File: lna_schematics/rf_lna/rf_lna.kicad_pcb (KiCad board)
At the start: 4 copper layers, 26 parts, among them J1 Conn_01x02_Pin, J2 Conn_Coaxial_Small, J3 Conn_Coaxial_Small, U1 L78L05_SOT89, U2 BFP640, U3 BFP640, U4 BFP640

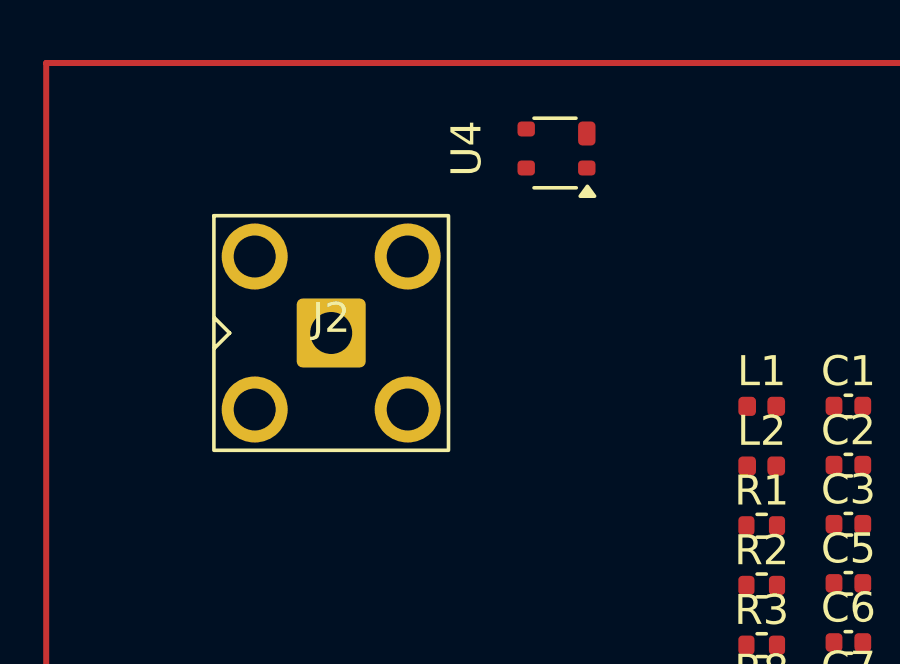
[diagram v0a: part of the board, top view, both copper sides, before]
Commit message: [kicad] Implemement custom design rule for CPW
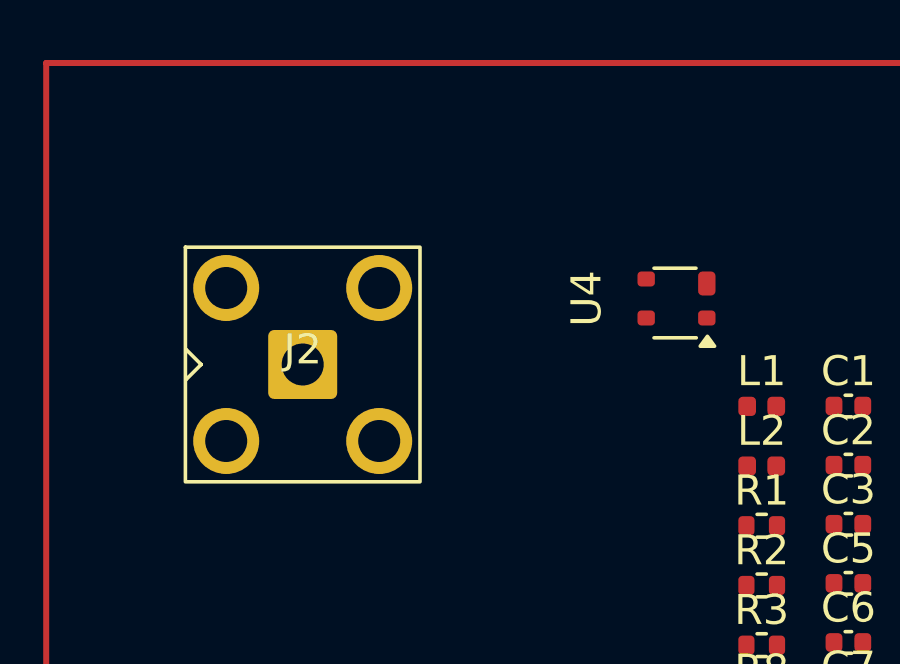
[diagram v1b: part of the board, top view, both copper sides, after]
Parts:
- moved U4 6.40 mm to (71.0, 57.9)
- moved J2 1.42 mm to (58.5, 60.0)
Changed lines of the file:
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@@
 	(footprint "Library:BFP640"
 		(layer "F.Cu")
-		(at 67.01 52.85 90)
+		(at 71.01 57.85 90)
 		(property "Reference" "U4"
 			(at 0 -3 90)
@@
 	(footprint "Library:SMA_Amphenol_901-143_Vertical"
 		(layer "F.Cu")
-		(at 59.5 59)
+		(at 58.55 60.05)
 		(property "Reference" "J2"
 			(at 0 -0.5 0)

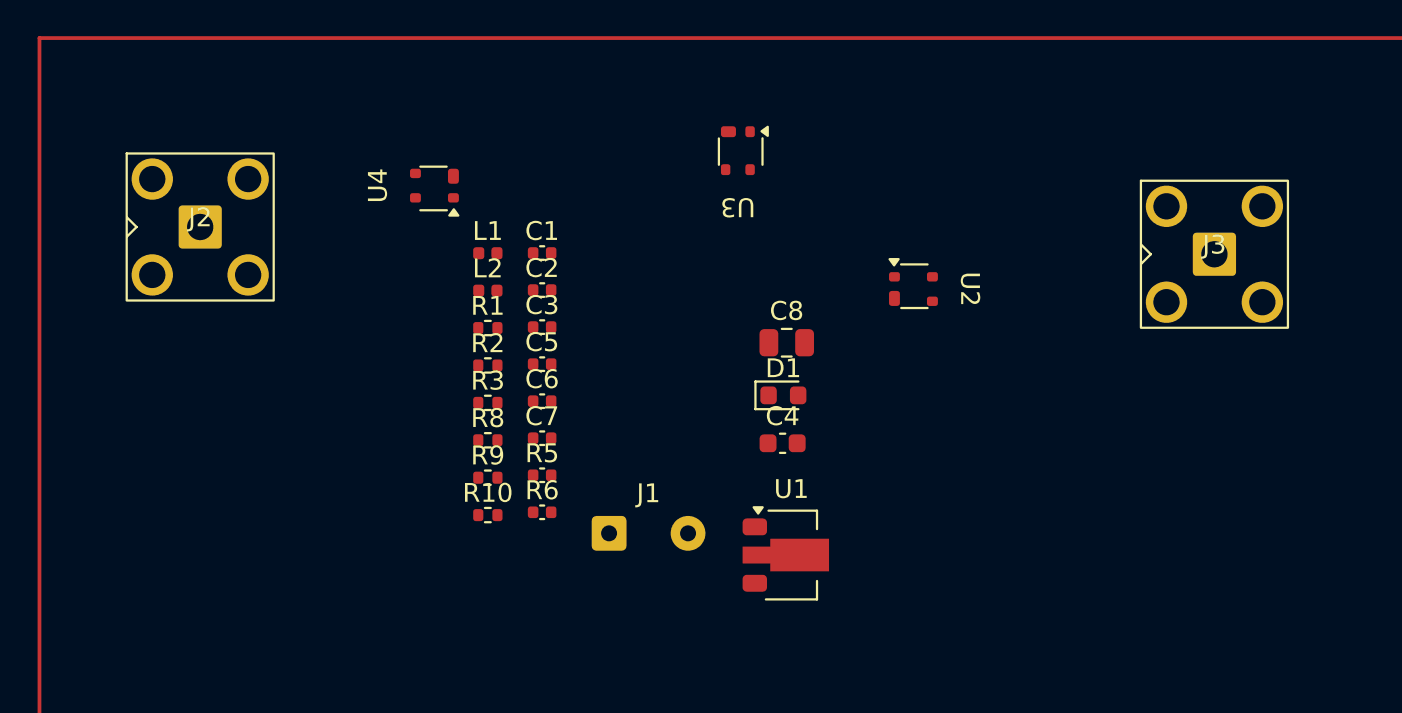
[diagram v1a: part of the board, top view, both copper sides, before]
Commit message: [lna_schematics] Added single-transistor LNA to schematics | TODO: update footprint and matched impedance with inductors
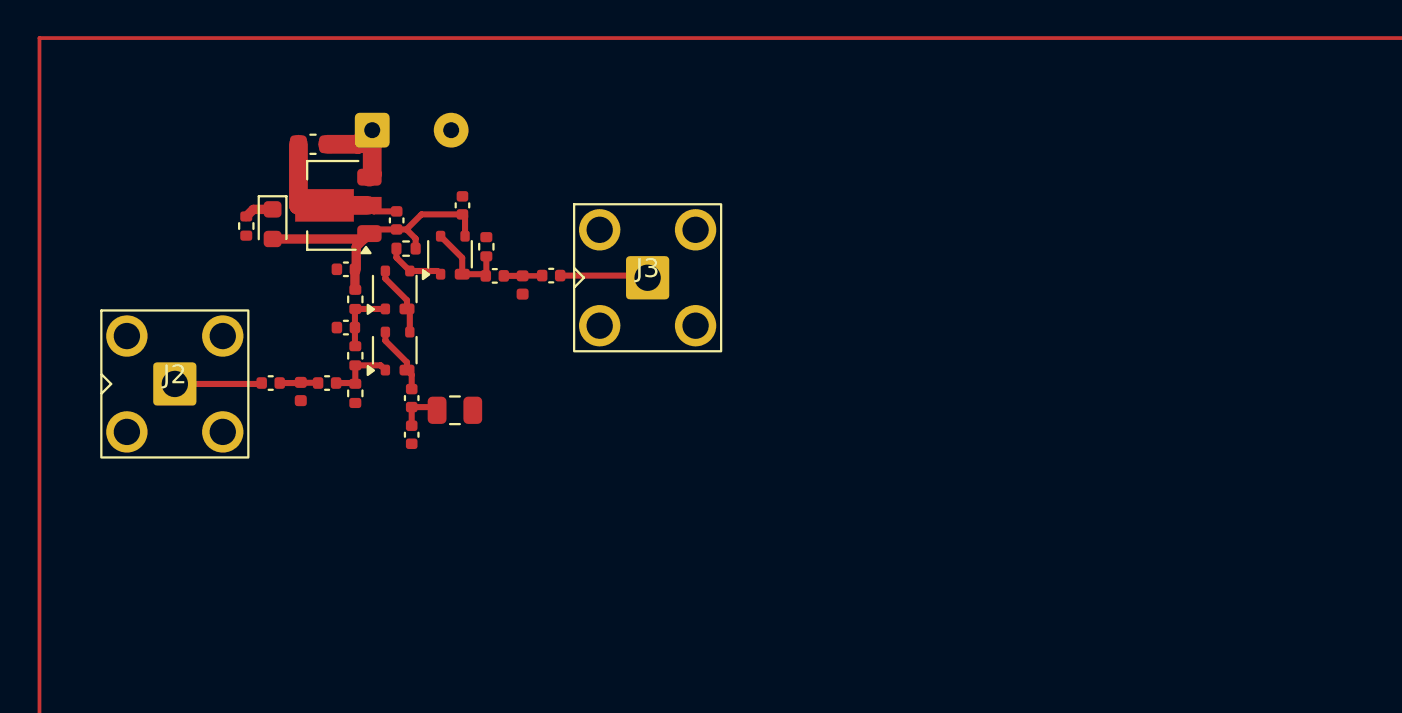
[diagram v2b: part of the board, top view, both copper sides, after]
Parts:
- added C10: 100pF, Capacitor_SMD:C_0402_1005Metric, F.Cu at (72.5, 58.9)
- added C9: 100pF, Capacitor_SMD:C_0402_1005Metric, F.Cu at (66.3, 65.4)
- moved U1 30.7 mm to (65.6, 58.9), turned to 180 degrees
- moved J3 30.2 mm to (82.3, 62.8)
- moved C1 29.6 mm to (64.5, 55.6), turned to 180 degrees
- moved D1 28.7 mm to (62.4, 59.9), turned to -90 degrees
- moved U2 27.4 mm to (69.0, 63.4), turned to 0 degrees
- moved J1 24.9 mm to (67.7, 54.9)
- moved C6 18.0 mm to (72.1, 69.8)
- moved R1 17.2 mm to (61.0, 60.0), turned to -90 degrees
- moved U3 16.1 mm to (72.0, 61.5), turned to 0 degrees
- moved C4 14.7 mm to (62.3, 68.3)
- moved C3 13.8 mm to (66.3, 62.3), turned to 180 degrees
- moved C5 13.4 mm to (65.3, 68.3)
- moved L1 12.4 mm to (63.9, 68.8), turned to -90 degrees
- moved C2 12.3 mm to (69.0, 59.7), turned to 90 degrees
- moved R5 11.0 mm to (66.8, 66.9), turned to -90 degrees
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- renumbered C4 to C1, C6 to C2, C7 to C3, C3 to C4, C1 to C5, C8 to C6, C5 to C7, C2 to C8, R8 to R1, R2 to R3, R1 to R4, R10 to R5, R9 to R6, R5 to R7, R6 to R8, R3 to R9
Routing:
- net GND: track 0.00 -> 60.2 mm
- net +5V: track 0.00 -> 16.2 mm
- net +BATT: track 0.00 -> 5.25 mm
- net /Out_emitter: track 0.00 -> 4.84 mm
- net /Output: track 0.00 -> 4.70 mm
- net /Input: track 0.00 -> 4.64 mm
- net Net-(U2-E): track 0.00 -> 3.79 mm
- net /In_base: track 0.00 -> 3.73 mm
- net Net-(U2-B): track 0.00 -> 3.71 mm
- net Net-(U4-E): track 0.00 -> 3.61 mm
- net Net-(U2-C): track 0.00 -> 3.19 mm
- net Net-(C6-Pad1): track 0.00 -> 2.44 mm
- net /In_match: track 0.00 -> 2.07 mm
- net /Out_match: track 0.00 -> 2.07 mm
- net Net-(D1-K): track 0.00 -> 1.56 mm
- added copper zone on In1.Cu, net GND
- added copper zone on In2.Cu, net GND

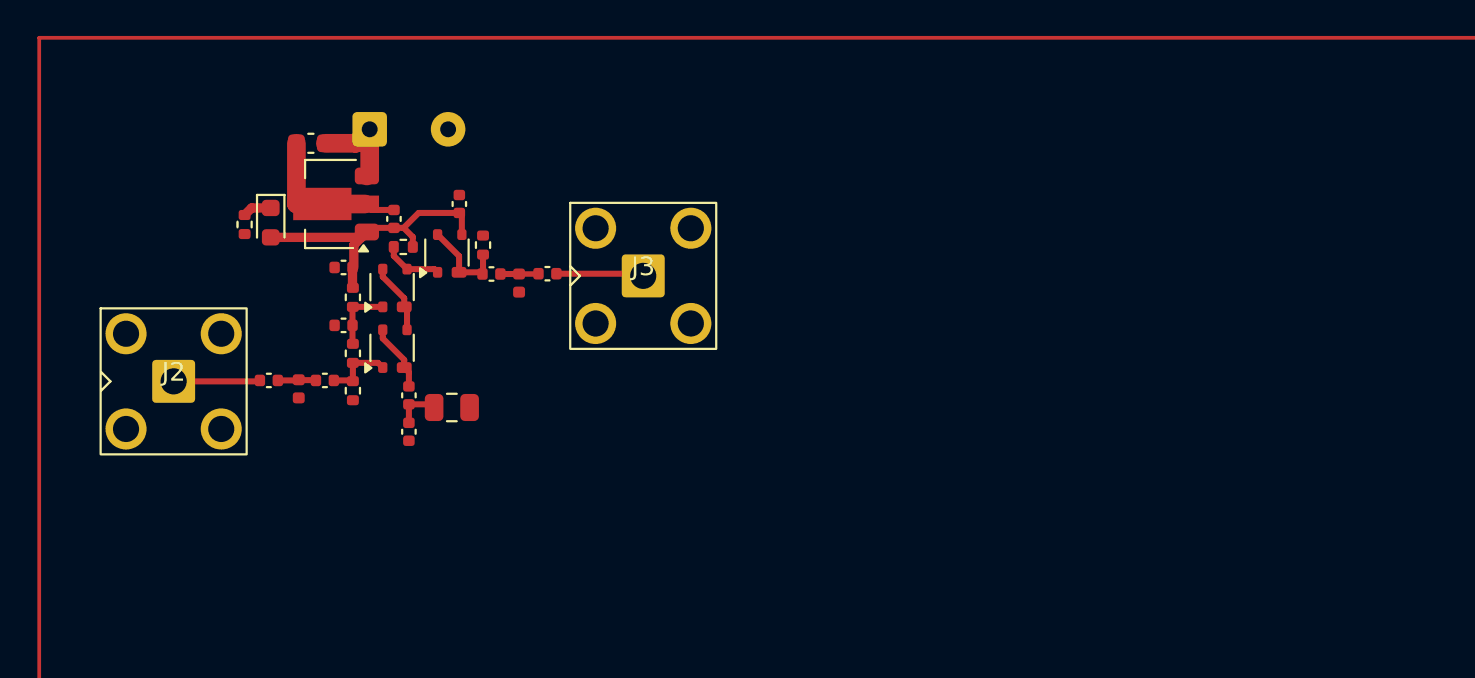
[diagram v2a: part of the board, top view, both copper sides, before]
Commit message: [rf_lna] did layout of rf amplifiers for LNA | TODO: create an antenna design for the bottom half
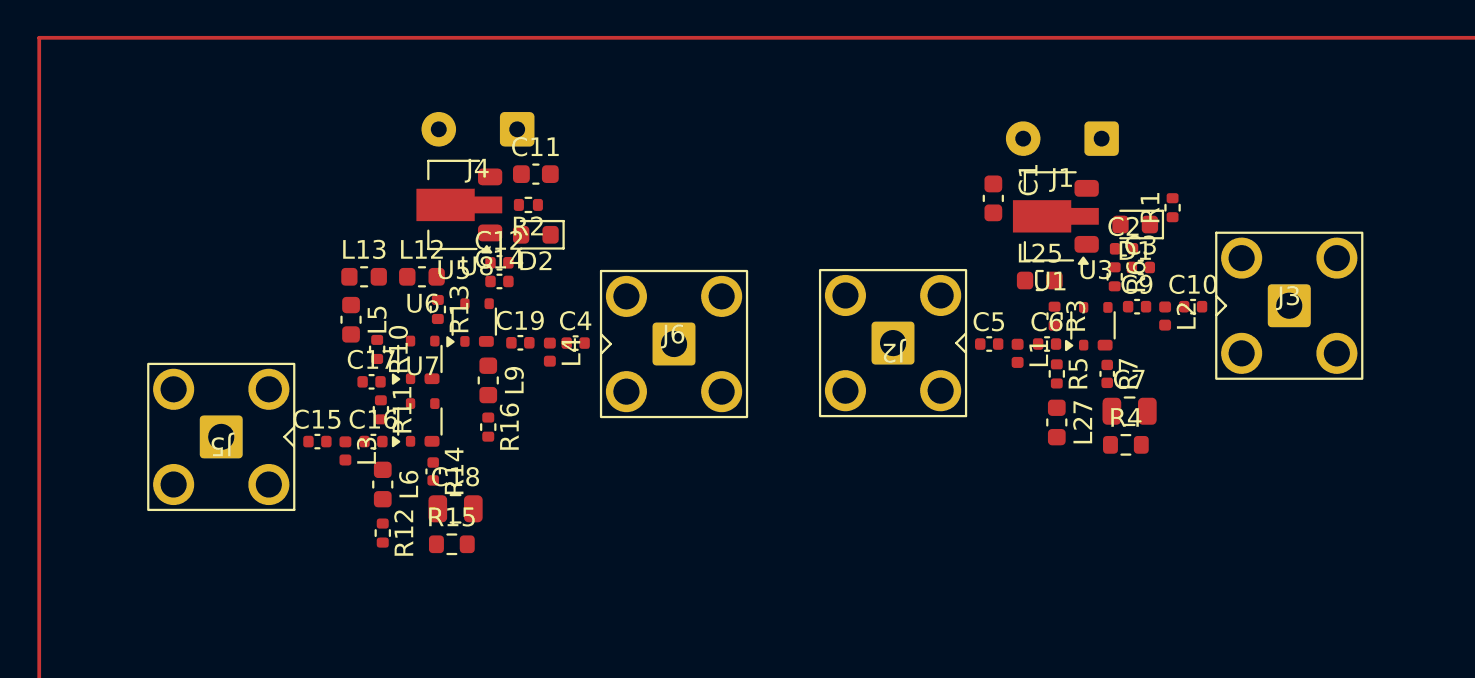
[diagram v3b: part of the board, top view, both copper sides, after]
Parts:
- removed C8: 1.2pF, Capacitor_SMD:C_0402_1005Metric
- removed R8: 47, Capacitor_SMD:C_0402_1005Metric
- removed R9: 200, Resistor_SMD:R_0402_1005Metric
- removed U2, U4: BFP640, Library:BFP640
- added C11: 470nF, Capacitor_SMD:C_0603_1608Metric, F.Cu at (76.6, 57.3)
- added C12: 100nF, Capacitor_SMD:C_0402_1005Metric, F.Cu at (74.7, 62.0)
- added C14: 100pF, Capacitor_SMD:C_0402_1005Metric, F.Cu at (74.7, 63.0)
- added C15: 1pF, Capacitor_SMD:C_0402_1005Metric, F.Cu at (64.9, 71.6)
- added C16: 3.6pF, Capacitor_SMD:C_0402_1005Metric, F.Cu at (67.9, 71.6)
- added C17: 100pF, Capacitor_SMD:C_0402_1005Metric, F.Cu at (67.8, 68.4)
- added C18: 2.2nF, Capacitor_SMD:C_0805_2012Metric, F.Cu at (72.3, 75.2)
- added C19: 3.6pF, Capacitor_SMD:C_0402_1005Metric, F.Cu at (75.8, 66.3)
- added D2: LED_Small, LED_SMD:LED_0603_1608Metric, F.Cu at (76.6, 60.5)
- added J4: Conn_01x02_Pin, Connector_Wire:SolderWire-0.25sqmm_1x02_P4.2mm_D0.65mm_OD1.7mm, F.Cu at (75.6, 54.9)
- added J5: Conn_Coaxial_Small, Library:SMA_Amphenol_901-143_Vertical, F.Cu at (59.8, 71.4)
- added J6: Conn_Coaxial_Small, Library:SMA_Amphenol_901-143_Vertical, F.Cu at (84.0, 66.4)
- added L12: 160nH, Inductor_SMD:L_0603_1608Metric, F.Cu at (70.5, 62.8)
- added L13: 160nH, Inductor_SMD:L_0603_1608Metric, F.Cu at (67.4, 62.8)
- added L25: 160nH, Inductor_SMD:L_0603_1608Metric, F.Cu at (103.6, 63.0)
- added L27: 160nH, Inductor_SMD:L_0603_1608Metric, F.Cu at (104.5, 70.6)
- added L3: 20nH, Inductor_SMD:L_0402_1005Metric, F.Cu at (66.4, 72.1)
- added L4: 15nH, Inductor_SMD:L_0402_1005Metric, F.Cu at (77.3, 66.8)
- added L5: 160nH, Inductor_SMD:L_0603_1608Metric, F.Cu at (66.7, 65.1)
- added L6: 160nH, Inductor_SMD:L_0603_1608Metric, F.Cu at (68.4, 73.9)
- added L9: 160nH, Inductor_SMD:L_0603_1608Metric, F.Cu at (74.0, 68.3)
- added R10: 2.2e3, Resistor_SMD:R_0402_1005Metric, F.Cu at (68.1, 66.7)
- added R11: 1e3, Resistor_SMD:R_0402_1005Metric, F.Cu at (68.3, 69.9)
- added R12: 1e3, Resistor_SMD:R_0402_1005Metric, F.Cu at (68.4, 76.5)
- added R13: 200, Resistor_SMD:R_0402_1005Metric, F.Cu at (71.3, 64.5)
- added R14: 0, Capacitor_SMD:C_0402_1005Metric, F.Cu at (71.1, 73.2)
- added R15: 47, Resistor_SMD:R_0603_1608Metric, F.Cu at (72.1, 77.1)
- added R16: 200, Resistor_SMD:R_0402_1005Metric, F.Cu at (74.0, 70.8)
- added R2: 1e3, Resistor_SMD:R_0402_1005Metric, F.Cu at (76.2, 59.0)
- added U5: L78L05_SOT89, Package_TO_SOT_SMD:SOT-89-3, F.Cu at (72.2, 59.0)
- added U6: BFP640, Library:BFP640, F.Cu at (70.5, 67.2)
- added U7: BFP640, Library:BFP640, F.Cu at (70.5, 70.6)
- added U8: BFP640, Library:BFP640, F.Cu at (73.5, 65.2)
- C10, C9: value 100pF -> 1pF
- C4: value 1.2pF -> 3.6pF
- C5: value 3.7pF -> 1pF
- C6: value 2.2nF -> 6.8pF; footprint Capacitor_SMD:C_0805_2012Metric -> Capacitor_SMD:C_0402_1005Metric
- C7: value 3.7pF -> 2.2nF; footprint Capacitor_SMD:C_0402_1005Metric -> Capacitor_SMD:C_0805_2012Metric
- L1: value 18nH -> 16nH
- L2: value 6.8nH -> 24nH
- R3: value 2.2e3 -> 1e3
- R4: value 200 -> 47; footprint Resistor_SMD:R_0402_1005Metric -> Resistor_SMD:R_0603_1608Metric
- R5: value 1e3 -> 330
- R6: value 1e3 -> 200
- moved R1 49.7 mm to (110.7, 59.1), turned to 90 degrees
- moved D1 46.3 mm to (108.7, 60.0), turned to 180 degrees
- moved C3 42.7 mm to (109.0, 62.3), turned to 0 degrees
- moved C9 42.5 mm to (108.8, 64.4)
- moved R6 41.3 mm to (107.6, 62.8)
- moved R4 40.1 mm to (108.2, 71.8), turned to 0 degrees
- moved C10 39.7 mm to (111.8, 64.4), turned to 0 degrees
- moved J1 39.2 mm to (106.9, 55.4), turned to 180 degrees
- moved C2 39.1 mm to (108.1, 61.3), turned to 0 degrees
- moved J2 38.6 mm to (95.7, 66.3), turned to 180 degrees
- moved U1 38.6 mm to (104.2, 59.6)
- moved L1 38.5 mm to (102.4, 66.9)
- moved R5 37.7 mm to (104.5, 68.0)
- moved R3 37.6 mm to (104.4, 64.9)
- moved R7 37.4 mm to (107.2, 68.0)
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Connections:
- net +BATT renamed +VDC
- C10 pad 1: +5V -> /lna/lna_out_match
- C10 pad 2: GND -> /lna/lna_out
- C2 pad 1: +5V -> +5C
- C3 pad 1: +5V -> +5C
- C4 pad 1: /Input -> /cascode/casc_out_match
- C4 pad 2: /In_match -> /cascode/casc_out
- C5 pad 1: /In_match -> /lna/lna_in
- C5 pad 2: /In_base -> /lna/lna_in_match
- C6 pad 1: Net-(C6-Pad1) -> /lna/lna_in_match
- C6 pad 2: GND -> /lna/lna_in_base
- C7 pad 1: /Out_emitter -> Net-(C7-Pad1)
- C7 pad 2: /Out_match -> GND
- C9 pad 1: GND -> /lna/lna_out_emitter
- C9 pad 2: Net-(U2-B) -> /lna/lna_out_match
- D1 pad 2: +5V -> +5C
- J2 pad 1: /Input -> /lna/lna_in
- J3 pad 1: /Output -> /lna/lna_out
- L1 pad 1: /In_match -> /lna/lna_in_match
- L2 pad 1: /Out_match -> /lna/lna_out_match
- R3 pad 1: +5V -> Net-(L25-Pad2)
- R3 pad 2: Net-(U2-B) -> /lna/lna_in_base
- R4 pad 1: +5V -> Net-(C7-Pad1)
- R4 pad 2: Net-(U2-C) -> GND
- R5 pad 1: Net-(U2-B) -> /lna/lna_in_base
- R5 pad 2: /In_base -> Net-(L27-Pad1)
- R6 pad 1: /In_base -> +5C
- R6 pad 2: GND -> /lna/lna_out_emitter
- R7 pad 1: Net-(U4-E) -> Net-(U3-E)
- R7 pad 2: Net-(C6-Pad1) -> Net-(C7-Pad1)
- U1 pad 1: +5V -> +5C
- U3 pad 1: Net-(U2-C) -> /lna/lna_in_base
- U3 pad 2: /Out_emitter -> Net-(U3-E)
- U3 pad 3: +5V -> /lna/lna_out_emitter
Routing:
- net GND: track 60.2 -> 20.4 mm
- net /cascode/casc_out: track 0.00 -> 30.9 mm
- net +5V: track 16.2 -> 0.00 mm
- net +VDC: track 5.25 -> 0.00 mm
- net /Out_emitter: track 4.84 -> 0.00 mm
- net /Output: track 4.70 -> 0.00 mm
- net /Input: track 4.64 -> 0.00 mm
- net Net-(U2-E): track 3.79 -> 0.00 mm
- net /In_base: track 3.73 -> 0.00 mm
- net Net-(U2-B): track 3.71 -> 0.00 mm
- net Net-(U4-E): track 3.61 -> 0.00 mm
- net Net-(U2-C): track 3.19 -> 0.00 mm
- net Net-(C6-Pad1): track 2.44 -> 0.00 mm
- net /In_match: track 2.07 -> 0.00 mm
- net /Out_match: track 2.07 -> 0.00 mm
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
